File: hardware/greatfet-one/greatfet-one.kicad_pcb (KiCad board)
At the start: 4 copper layers, 70.6 x 53.3 mm, 99 parts, among them J1 NEIGHBOR1, J2 NEIGHBOR2, J3 USB-MICRO-B-SHIELDED, J4 USB-MICRO-B-SHIELDED, J5 JTAG, J6 POWER, J7 BONUS_ROW, SW1 DFU, SW2 RESET, U1 LPC4330FBD144, U2 W25Q16DV, U3 AP7333, U4 IP4220CZ6, U5 AP2553W6-7, X1 MCU_XTAL, X2 RTC_XTAL

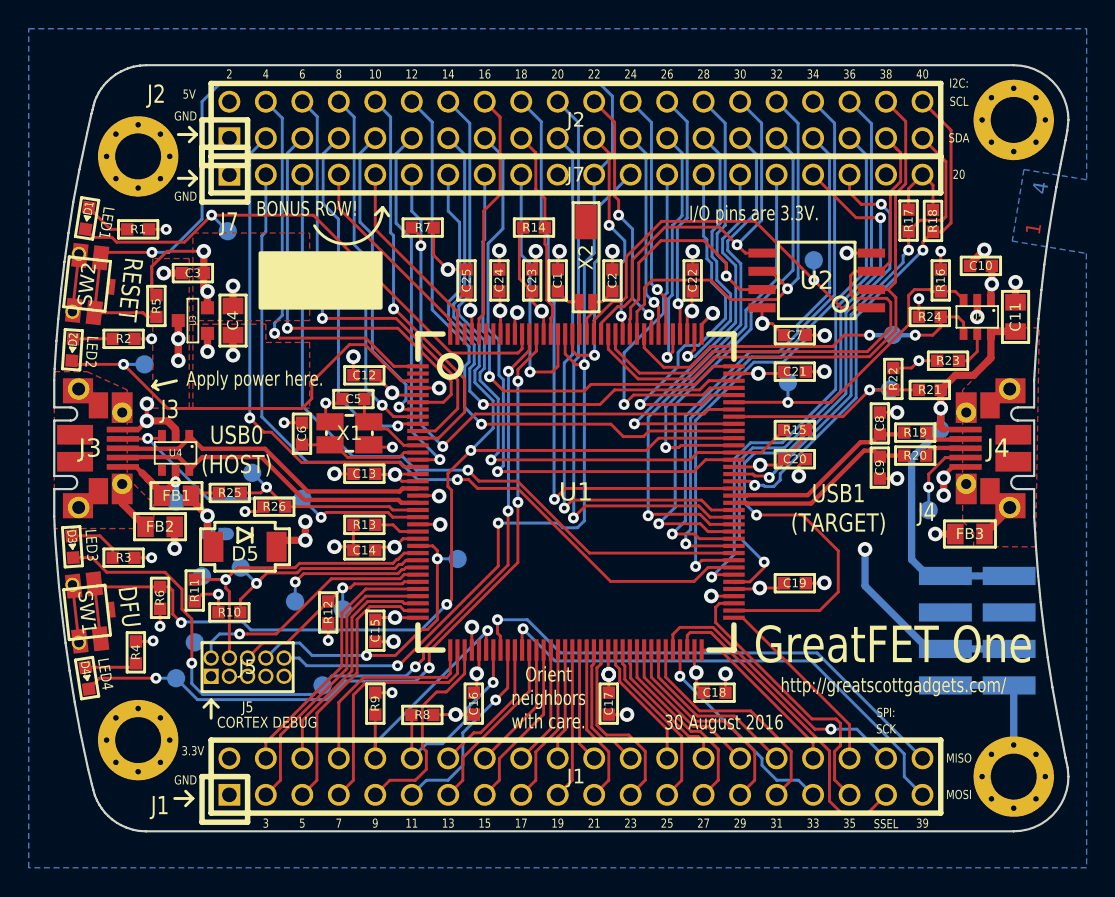
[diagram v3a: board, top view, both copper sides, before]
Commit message: GreatFET One: minor routing tweaks to improve +5V zone
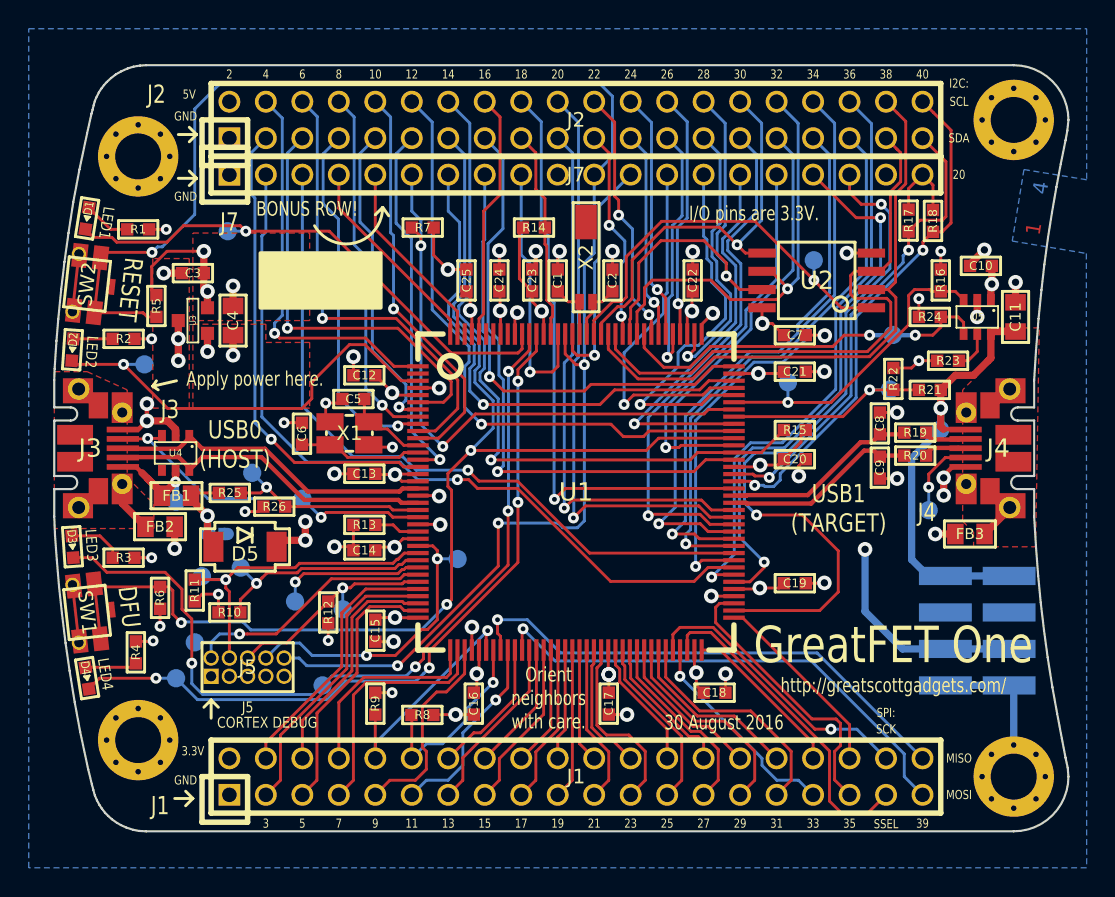
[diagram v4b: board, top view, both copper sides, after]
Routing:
- net VCC: track 103.9 -> 104.9 mm
- net /LED1: track 38.3 -> 37.3 mm
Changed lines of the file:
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@@
     (links 374)
     (no_connects 0)
-    (area 105.842999 71.044999 176.605001 124.535001)
+    (area 93.271704 68.58 207.466001 199.465001)
     (thickness 1.6)
     (drawings 228)
-    (tracks 1526)
+    (tracks 1530)
     (zones 0)
     (modules 99)
@@
     (1 C2.Cu power hide)
     (2 C3.Cu power hide)
-    (31 B.Cu signal)
+    (31 B.Cu signal hide)
     (32 B.Adhes user)
     (33 F.Adhes user)
@@
   )
   (setup
-    (last_trace_width 0.2032)
+    (last_trace_width 0.508)
     (user_trace_width 0.3048)
     (user_trace_width 0.508)
@@
     (effects (font (size 0.635 0.508) (thickness 0.1016)) (justify mirror))
   )
-  (gr_text "TP3\nLED1" (at 119.888 82.677) (layer B.SilkS)
+  (gr_text "TP3\nLED1" (at 116.078 82.423) (layer B.SilkS)
     (effects (font (size 0.635 0.508) (thickness 0.1016)) (justify mirror))
   )
@@
     (effects (font (size 1.27 1.016) (thickness 0.2032)))
   )
-  (gr_text "USB0\n(HOST)" (at 118.618 97.917) (layer F.SilkS)
+  (gr_text "USB0\n(HOST)" (at 118.491 97.536) (layer F.SilkS)
     (effects (font (size 1.27 1.016) (thickness 0.2032)))
   )
@@
   (segment (start 142.48892 89.83726) (end 142.48892 87.59708) (width 0.2032) (layer F.Cu) (net 3) (status 30))
   (segment (start 142.48892 87.59708) (end 142.494 87.592) (width 0.2032) (layer F.Cu) (net 3) (status 30))
+  (segment (start 167.96 111.76) (end 172.4 111.76) (width 0.508) (layer B.Cu) (net 4))
+  (segment (start 162.3695 109.1565) (end 164.973 111.76) (width 0.508) (layer B.Cu) (net 4))
+  (segment (start 164.973 111.76) (end 167.96 111.76) (width 0.508) (layer B.Cu) (net 4))
+  (segment (start 162.3695 104.8258) (end 162.3695 109.1565) (width 0.508) (layer B.Cu) (net 4))
   (segment (start 117.348 107.95) (end 116.205 107.95) (width 0.2032) (layer F.Cu) (net 4))
   (segment (start 116.205 107.95) (end 115.697 108.458) (width 0.2032) (layer F.Cu) (net 4))
@@
   (via (at 139.8524 88.2396) (size 1.016) (drill 0.508) (layers F.Cu B.Cu) (net 4))
   (via (at 112.8 111.2) (size 0.762) (drill 0.3302) (layers F.Cu B.Cu) (net 4))
-  (segment (start 162.3695 107.3745) (end 162.3695 104.8258) (width 0.508) (layer B.Cu) (net 4))
   (segment (start 135.49122 113.32718) (end 135.3312 113.4872) (width 0.2032) (layer F.Cu) (net 4))
   (segment (start 135.3312 113.4872) (end 135.3312 114.6048) (width 0.2032) (layer F.Cu) (net 4) (status 20))
-  (segment (start 166.755 111.76) (end 162.3695 107.3745) (width 0.508) (layer B.Cu) (net 4))
   (segment (start 144.49044 113.50244) (end 144.526 113.538) (width 0.2032) (layer F.Cu) (net 4))
   (segment (start 144.49044 111.83874) (end 144.49044 113.50244) (width 0.2032) (layer F.Cu) (net 4) (status 10))
@@
   (segment (start 129.6543 109.5883) (end 129.6416 109.5756) (width 0.2032) (layer F.Cu) (net 4))
   (segment (start 131.23926 109.5883) (end 129.6543 109.5883) (width 0.2032) (layer F.Cu) (net 4) (status 10))
-  (segment (start 167.96 111.76) (end 166.755 111.76) (width 0.508) (layer B.Cu) (net 4))
   (segment (start 149.98954 89.83726) (end 149.98954 88.56726) (width 0.2032) (layer F.Cu) (net 4) (status 10))
   (segment (start 150.3172 86.9188) (end 150.368 86.868) (width 0.2032) (layer F.Cu) (net 4) (status 30))
@@
   (segment (start 135.49122 111.83874) (end 135.49122 113.32718) (width 0.2032) (layer F.Cu) (net 4) (status 10))
   (segment (start 128.3208 99.6188) (end 128.27 99.568) (width 0.2032) (layer F.Cu) (net 4) (status 30))
-  (segment (start 172.4 111.76) (end 167.96 111.76) (width 0.508) (layer B.Cu) (net 4))
   (segment (start 136.98982 88.24722) (end 136.9568 88.2142) (width 0.2032) (layer F.Cu) (net 4))
   (segment (start 136.9568 86.9188) (end 136.906 86.868) (width 0.2032) (layer F.Cu) (net 4) (status 30))
@@
   (segment (start 108.323203 81.035381) (end 109.837822 82.55) (width 0.2032) (layer F.Cu) (net 8))
   (segment (start 109.837822 82.55) (end 110.998 82.55) (width 0.2032) (layer F.Cu) (net 8))
-  (segment (start 117.9957 82.677) (end 117.99316 82.677) (width 0.2032) (layer B.Cu) (net 9))
-  (segment (start 117.99316 82.677) (end 116.87556 81.5594) (width 0.2032) (layer B.Cu) (net 9))
-  (segment (start 133.5532 91.1606) (end 123.952002 81.5594) (width 0.2032) (layer F.Cu) (net 9))
-  (segment (start 123.952002 81.5594) (end 116.87556 81.5594) (width 0.2032) (layer F.Cu) (net 9))
-  (segment (start 110.2614 83.439) (end 114.99596 83.439) (width 0.2032) (layer F.Cu) (net 9))
-  (segment (start 114.99596 83.439) (end 116.87556 81.5594) (width 0.2032) (layer F.Cu) (net 9))
-  (via (at 116.87556 81.5594) (size 0.762) (drill 0.3302) (layers F.Cu B.Cu) (net 9))
+  (segment (start 119.253 82.677) (end 118.872001 82.296001) (width 0.2032) (layer F.Cu) (net 9))
   (segment (start 110.2614 83.439) (end 109.9312 83.1088) (width 0.2032) (layer F.Cu) (net 9))
-  (segment (start 109.9312 83.1088) (end 108.652978 83.1088) (width 0.2032) (layer F.Cu) (net 9))
+  (segment (start 118.872001 82.296001) (end 114.909601 82.296001) (width 0.2032) (layer F.Cu) (net 9))
+  (segment (start 114.909601 82.296001) (end 113.766602 83.439) (width 0.2032) (layer F.Cu) (net 9))
   (segment (start 108.652978 83.1088) (end 108.084797 82.540619) (width 0.2032) (layer F.Cu) (net 9))
+  (segment (start 113.766602 83.439) (end 110.2614 83.439) (width 0.2032) (layer F.Cu) (net 9))
+  (segment (start 109.9312 83.1088) (end 108.652978 83.1088) (width 0.2032) (layer F.Cu) (net 9))
+  (segment (start 133.5532 91.1606) (end 125.069602 82.677) (width 0.2032) (layer F.Cu) (net 9))
+  (segment (start 125.069602 82.677) (end 119.253 82.677) (width 0.2032) (layer F.Cu) (net 9))
+  (segment (start 117.9957 82.677) (end 119.253 82.677) (width 0.2032) (layer B.Cu) (net 9))
+  (via (at 119.253 82.677) (size 0.762) (drill 0.3302) (layers F.Cu B.Cu) (net 9))
   (segment (start 138.49096 90.87104) (end 138.2014 91.1606) (width 0.2032) (layer F.Cu) (net 9))
   (segment (start 138.49096 89.83726) (end 138.49096 90.87104) (width 0.2032) (layer F.Cu) (net 9) (status 10))
@@
   (segment (start 138.49096 110.42904) (end 138.557 110.363) (width 0.2032) (layer F.Cu) (net 53))
   (via (at 138.557 110.363) (size 0.762) (drill 0.3302) (layers F.Cu B.Cu) (net 53))
+  (segment (start 120.65 76.2) (end 119.633999 77.216001) (width 0.2032) (layer B.Cu) (net 54))
+  (segment (start 119.633999 77.216001) (end 119.633999 80.114139) (width 0.2032) (layer B.Cu) (net 54))
+  (segment (start 119.633999 80.114139) (end 119.888001 80.368141) (width 0.2032) (layer B.Cu) (net 54))
+  (segment (start 119.888001 80.368141) (end 119.888001 96.021041) (width 0.2032) (layer B.Cu) (net 54))
+  (segment (start 119.888001 96.021041) (end 121.02648 97.15952) (width 0.2032) (layer B.Cu) (net 54))
+  (segment (start 123.139202 98.780602) (end 122.647562 98.780602) (width 0.2032) (layer F.Cu) (net 54))
+  (segment (start 122.647562 98.780602) (end 121.02648 97.15952) (width 0.2032) (layer F.Cu) (net 54))
+  (via (at 121.02648 97.15952) (size 0.762) (drill 0.3302) (layers F.Cu B.Cu) (net 54))
   (segment (start 130.22834 99.08794) (end 129.921002 98.780602) (width 0.2032) (layer F.Cu) (net 54))
   (segment (start 131.23926 99.08794) (end 130.22834 99.08794) (width 0.2032) (layer F.Cu) (net 54) (status 10))
-  (via (at 119.5324 95.6818) (size 0.762) (drill 0.3302) (layers F.Cu B.Cu) (net 54))
-  (segment (start 119.5324 77.3176) (end 119.5324 95.6818) (width 0.2032) (layer B.Cu) (net 54))
-  (segment (start 119.5324 77.3176) (end 120.65 76.2) (width 0.2032) (layer B.Cu) (net 54))
-  (segment (start 120.523 96.6724) (end 119.5324 95.6818) (width 0.2032) (layer F.Cu) (net 54))
-  (segment (start 121.031 96.6724) (end 120.523 96.6724) (width 0.2032) (layer F.Cu) (net 54))
-  (segment (start 123.139202 98.780602) (end 121.031 96.6724) (width 0.2032) (layer F.Cu) (net 54))
   (segment (start 129.921002 98.780602) (end 123.139202 98.780602) (width 0.2032) (layer F.Cu) (net 54))
   (segment (start 129.7178 82.1182) (end 129.7178 77.2922) (width 0.2032) (layer B.Cu) (net 55))
@@
   (segment (start 132.27304 104.58704) (end 132.588 104.902) (width 0.2032) (layer F.Cu) (net 100))
   (segment (start 131.23926 104.58704) (end 132.27304 104.58704) (width 0.2032) (layer F.Cu) (net 100) (status 10))
+  (segment (start 115.697 74.168) (end 115.697 81.508602) (width 0.2032) (layer B.Cu) (net 101))
+  (segment (start 115.697 81.508602) (end 113.436401 83.769201) (width 0.2032) (layer B.Cu) (net 101))
+  (segment (start 113.436401 83.769201) (end 113.106199 83.769201) (width 0.2032) (layer B.Cu) (net 101))
+  (segment (start 113.106199 83.769201) (end 112.7252 84.1502) (width 0.2032) (layer B.Cu) (net 101))
+  (segment (start 117.475 72.39) (end 115.697 74.168) (width 0.2032) (layer B.Cu) (net 101))
   (segment (start 109.516671 84.1502) (end 112.7252 84.1502) (width 0.2032) (layer F.Cu) (net 101))
   (segment (start 144.78 77.47) (end 144.78 73.279) (width 0.2032) (layer B.Cu) (net 101))
   (segment (start 144.78 73.279) (end 143.891 72.39) (width 0.2032) (layer B.Cu) (net 101))
   (segment (start 143.891 72.39) (end 117.475 72.39) (width 0.2032) (layer B.Cu) (net 101))
-  (segment (start 117.475 72.39) (end 116.205 73.66) (width 0.2032) (layer B.Cu) (net 101))
-  (segment (start 116.205 81.8388) (end 116.205 73.66) (width 0.2032) (layer B.Cu) (net 101))
-  (segment (start 113.8936 84.1502) (end 116.205 81.8388) (width 0.2032) (layer B.Cu) (net 101))
-  (segment (start 112.7252 84.1502) (end 113.8936 84.1502) (width 0.2032) (layer B.Cu) (net 101))
   (via (at 112.7252 84.1502) (size 0.762) (drill 0.3302) (layers F.Cu B.Cu) (net 101))
   (segment (start 144.78 77.47) (end 143.51 78.74) (width 0.2032) (layer B.Cu) (net 101) (status 10))

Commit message: GreatFET One: Changed resistor values to fix voltage dividers for USB0 and USB1 VBUS sensing.
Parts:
- R21, R25: value 10k -> 0
- R22, R26: value 18k -> 10k
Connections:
- J5 pad 7: Net-(J5-Pad7) -> (no net)
- U1 pad 136: Net-(U1-Pad136) -> (no net)
- U1 pad 138: Net-(U1-Pad138) -> (no net)
- U1 pad 139: Net-(U1-Pad139) -> (no net)
- U1 pad 142: Net-(U1-Pad142) -> (no net)
- U1 pad 2: Net-(U1-Pad2) -> (no net)
- U4 pad 4: Net-(U4-Pad4) -> (no net)

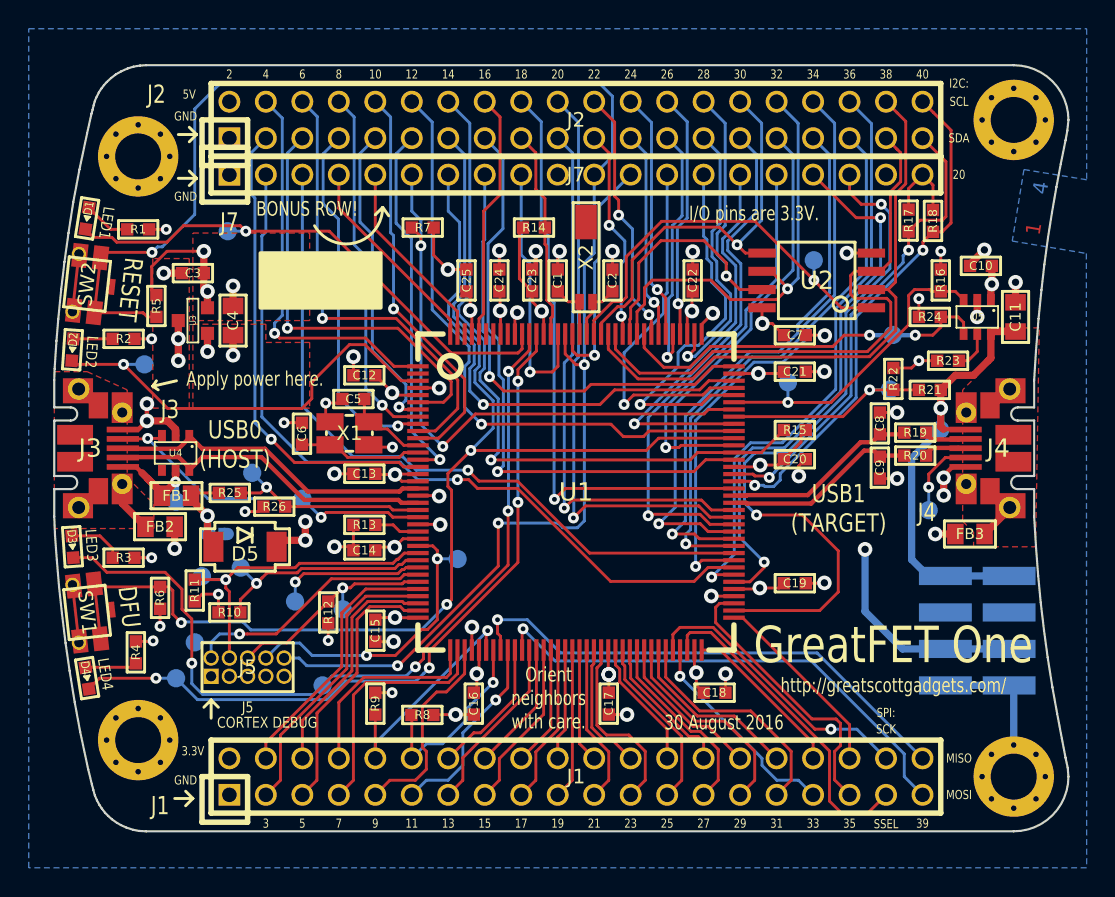
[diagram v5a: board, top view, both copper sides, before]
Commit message: GreatFET One: moved J5 for additional clearance needed for enclosure
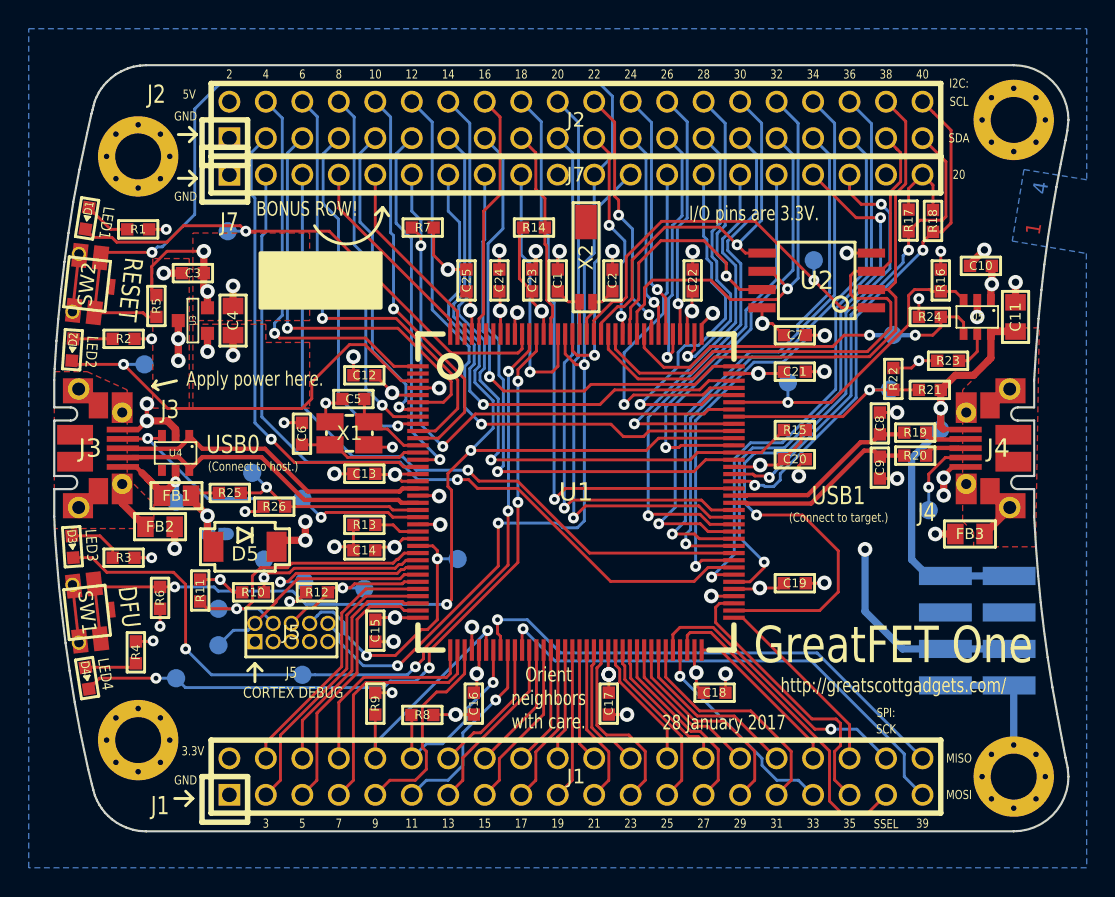
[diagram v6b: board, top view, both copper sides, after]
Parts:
- moved J5 3.89 mm to (122.4, 110.6)
- moved TP17 2.54 mm to (117.3, 109.0)
- moved R10 2.16 mm to (119.8, 107.8)
- moved TP18 2.08 mm to (127.5, 107.6)
- moved TP1 1.72 mm to (120.5, 105.5)
- moved TP16 1.66 mm to (117.3, 111.5)
- moved R12 1.60 mm to (124.2, 107.8), turned to 0 degrees
- moved TP5 1.59 mm to (123.2, 113.6)
- moved TP2 1.53 mm to (123.3, 107.1)
- moved R11 0.38 mm to (116.1, 107.7), turned to 270 degrees
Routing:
- net /TDO: track 15.6 -> 11.6 mm
- net /TMS: track 18.6 -> 16.0 mm, vias 1 -> 0
- net /P2_8: track 86.3 -> 83.8 mm
- net /DBGEN: track 15.9 -> 13.5 mm
- net /LED3: track 58.5 -> 56.5 mm
- net /TDI: track 21.5 -> 19.6 mm
- net /RESET: track 114.4 -> 112.6 mm
- net /TCK: track 23.6 -> 22.3 mm
- net /TRST: track 10.3 -> 11.7 mm
- net /LED4: track 51.9 -> 51.2 mm
- net VCC: track 104.9 -> 105.5 mm
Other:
- board text added: "(Connect to host.)"
- board text added: "(Connect to target.)"
- board text added: "28 January 2017"
- board text added: "USB0"
- board text added: "USB1"
- board text removed: "30 August 2016"
- board text removed: "USB0 (HOST)"
- board text removed: "USB1 (TARGET)"
